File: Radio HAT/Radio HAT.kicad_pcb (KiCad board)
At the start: 4 copper layers, 65 x 45 mm, 29 parts, among them J1 Raspberry_Pi_2_3, J2 Coax SMA, J3 Barrel_Jack, J4 VCC, J5 6V, J6 GND, J7 V_RF, U1 RFM98PW, U2 AZ2185D-ADJTRG1

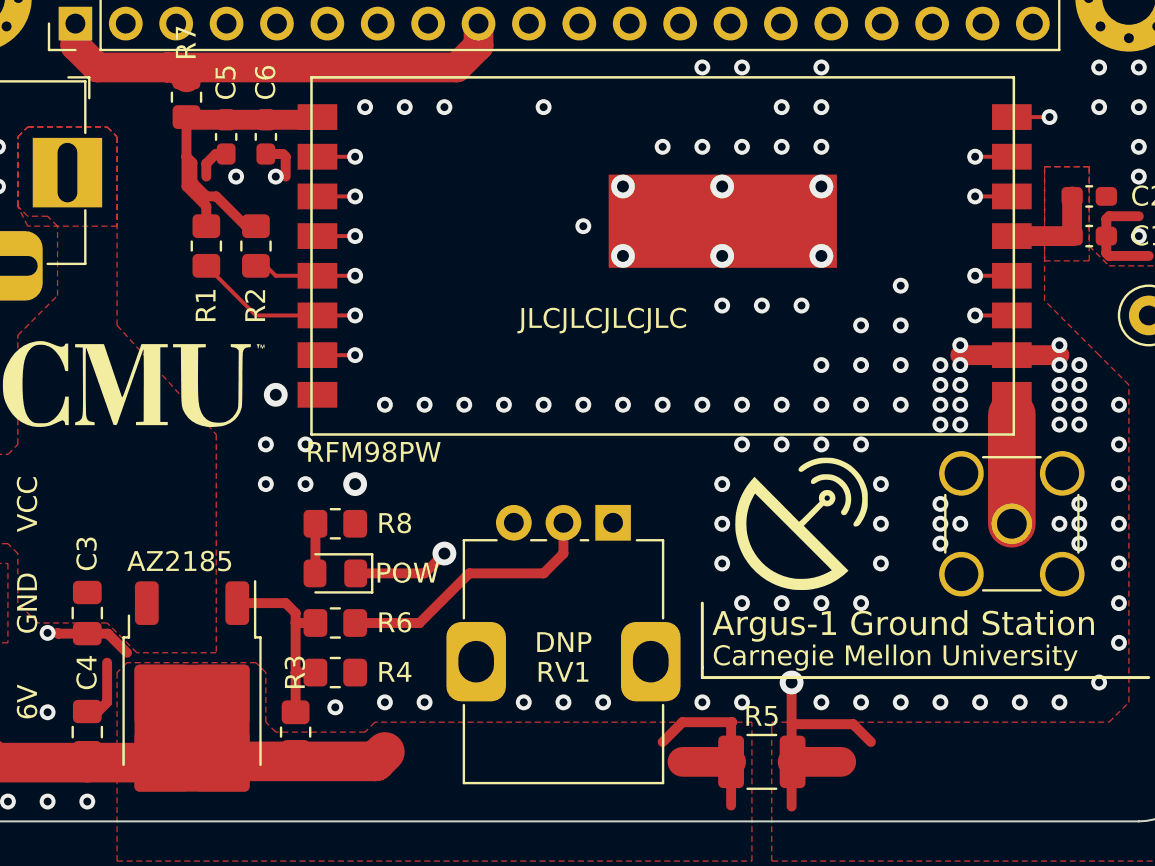
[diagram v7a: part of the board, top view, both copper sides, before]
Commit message: Impedance matched ANT trace
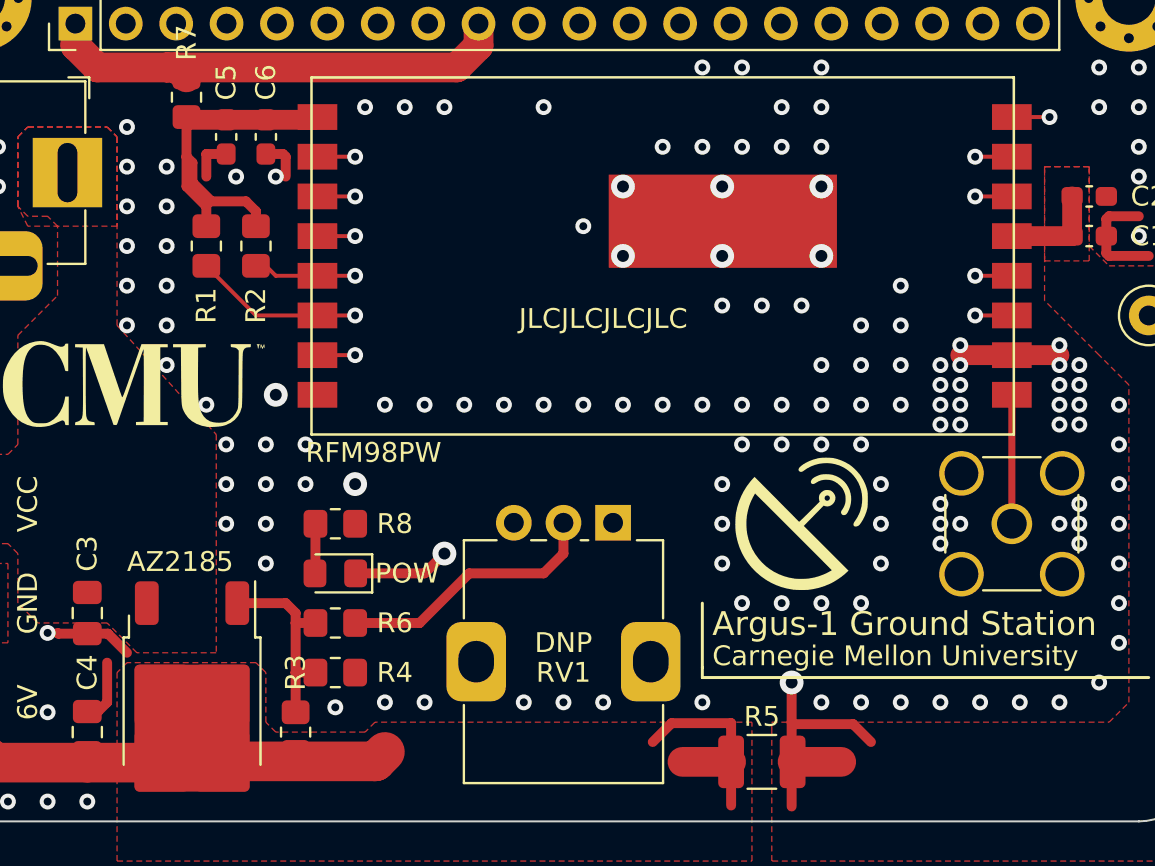
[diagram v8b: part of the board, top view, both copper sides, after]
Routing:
- net GND: track 21.6 -> 21.9 mm, vias 147 -> 164
